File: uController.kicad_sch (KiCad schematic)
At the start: 1 part

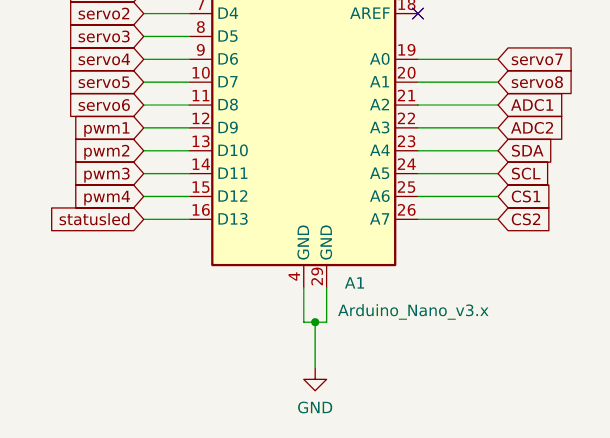
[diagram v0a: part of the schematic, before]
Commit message: redone the switch connectors to accomodate a current sense print. Rearranged parts and updated silk texts to be 50% of their original size
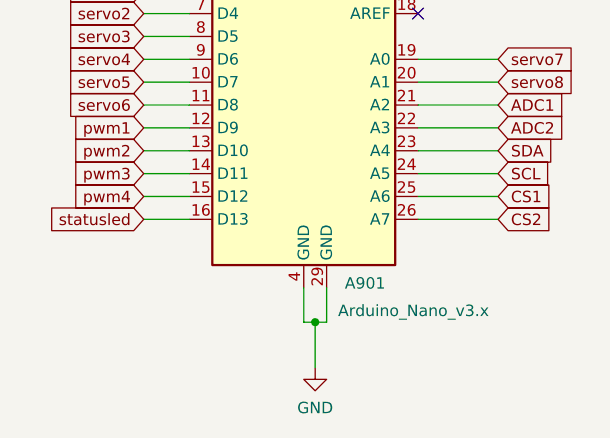
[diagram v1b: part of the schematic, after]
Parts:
- renumbered A1 to A901
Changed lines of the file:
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@@
   (symbol (lib_id "power:GND") (at 149.86 128.27 0) (unit 1)
     (in_bom yes) (on_board yes) (fields_autoplaced)
-    (property "Reference" "#PWR0132" (id 0) (at 149.86 134.62 0)
+    (property "Reference" "#PWR0901" (id 0) (at 149.86 134.62 0)
       (effects (font (size 1.27 1.27)) hide)
     )
@@
   (symbol (lib_id "MCU_Module:Arduino_Nano_v3.x") (at 148.59 93.98 0) (unit 1)
     (in_bom yes) (on_board yes)
-    (property "Reference" "A1" (id 0) (at 153.1494 118.8704 0)
+    (property "Reference" "A901" (id 0) (at 153.1494 118.8704 0)
       (effects (font (size 1.27 1.27)) (justify left))
     )
@@
   (symbol (lib_id "power:+5V") (at 153.67 64.77 0) (unit 1)
     (in_bom yes) (on_board yes) (fields_autoplaced)
-    (property "Reference" "#PWR0141" (id 0) (at 153.67 68.58 0)
+    (property "Reference" "#PWR0902" (id 0) (at 153.67 68.58 0)
       (effects (font (size 1.27 1.27)) hide)
     )

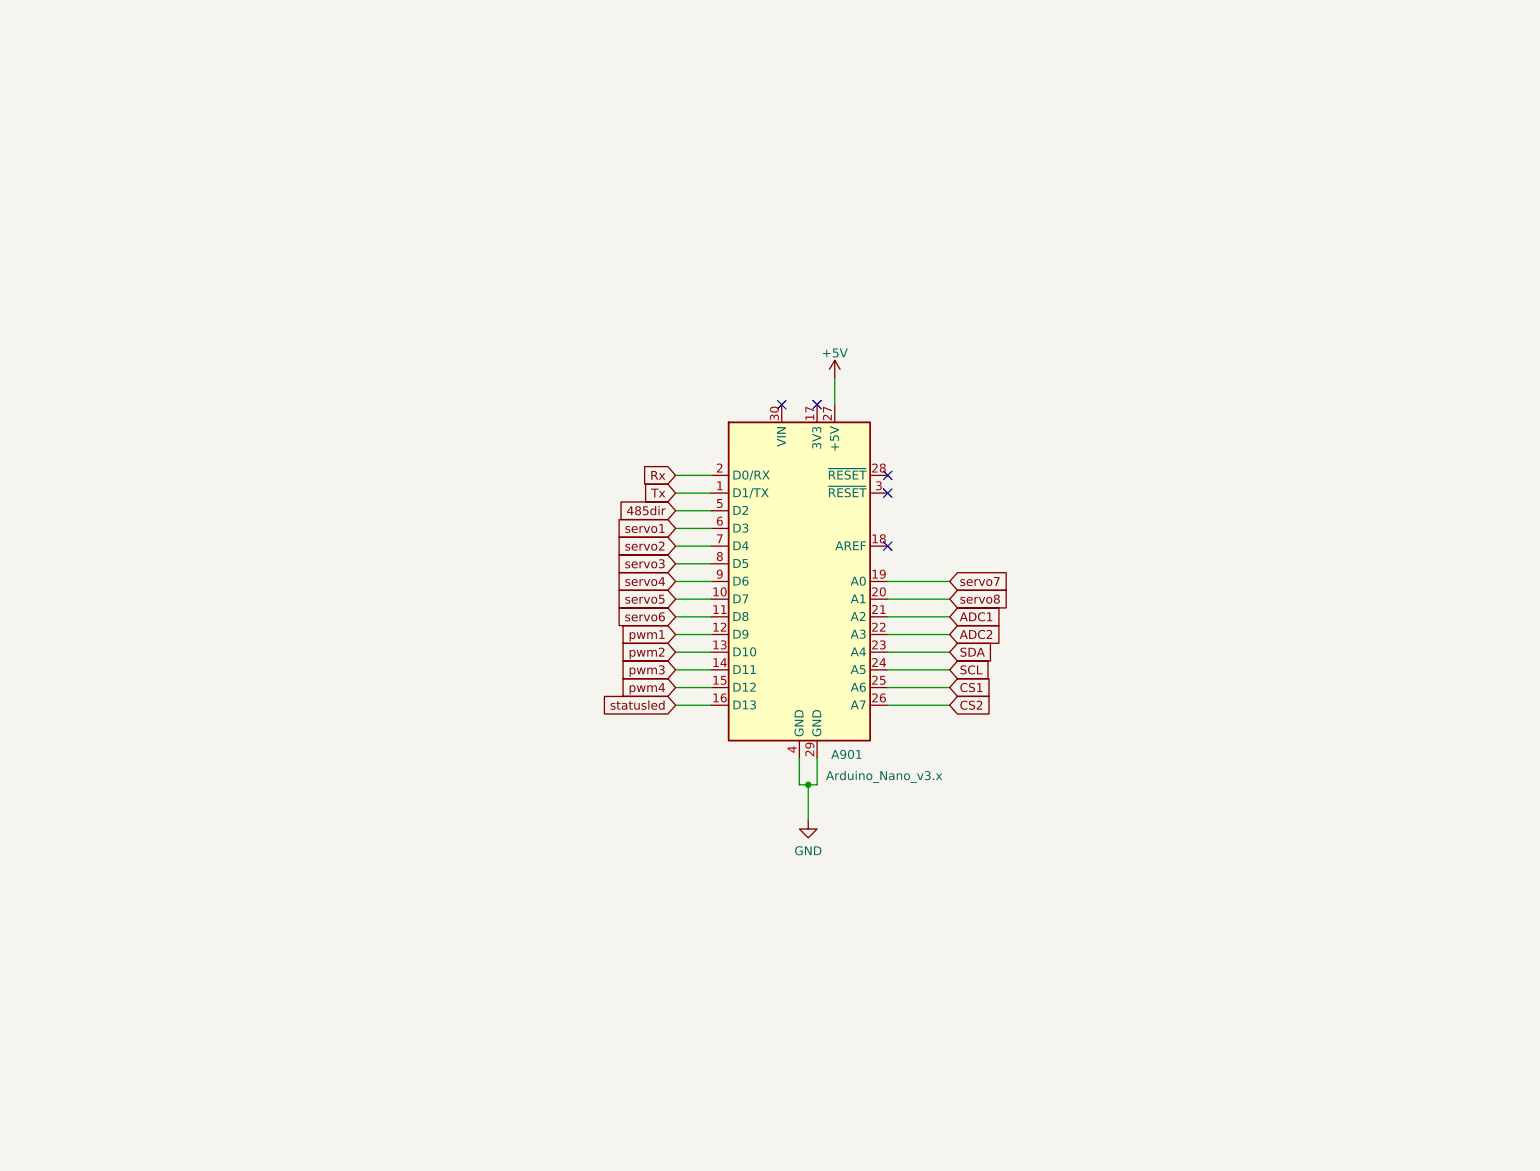
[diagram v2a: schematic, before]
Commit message: altered the code drastically and made a new PCB. PCB is still much work.
I finally fixed that issue where loco functions and speed were not serviced to the multimaus clients.
The Nx code also has been succesfully tested using the monitor.
MCP bug also has been solded. The bug was in assembleIO.py
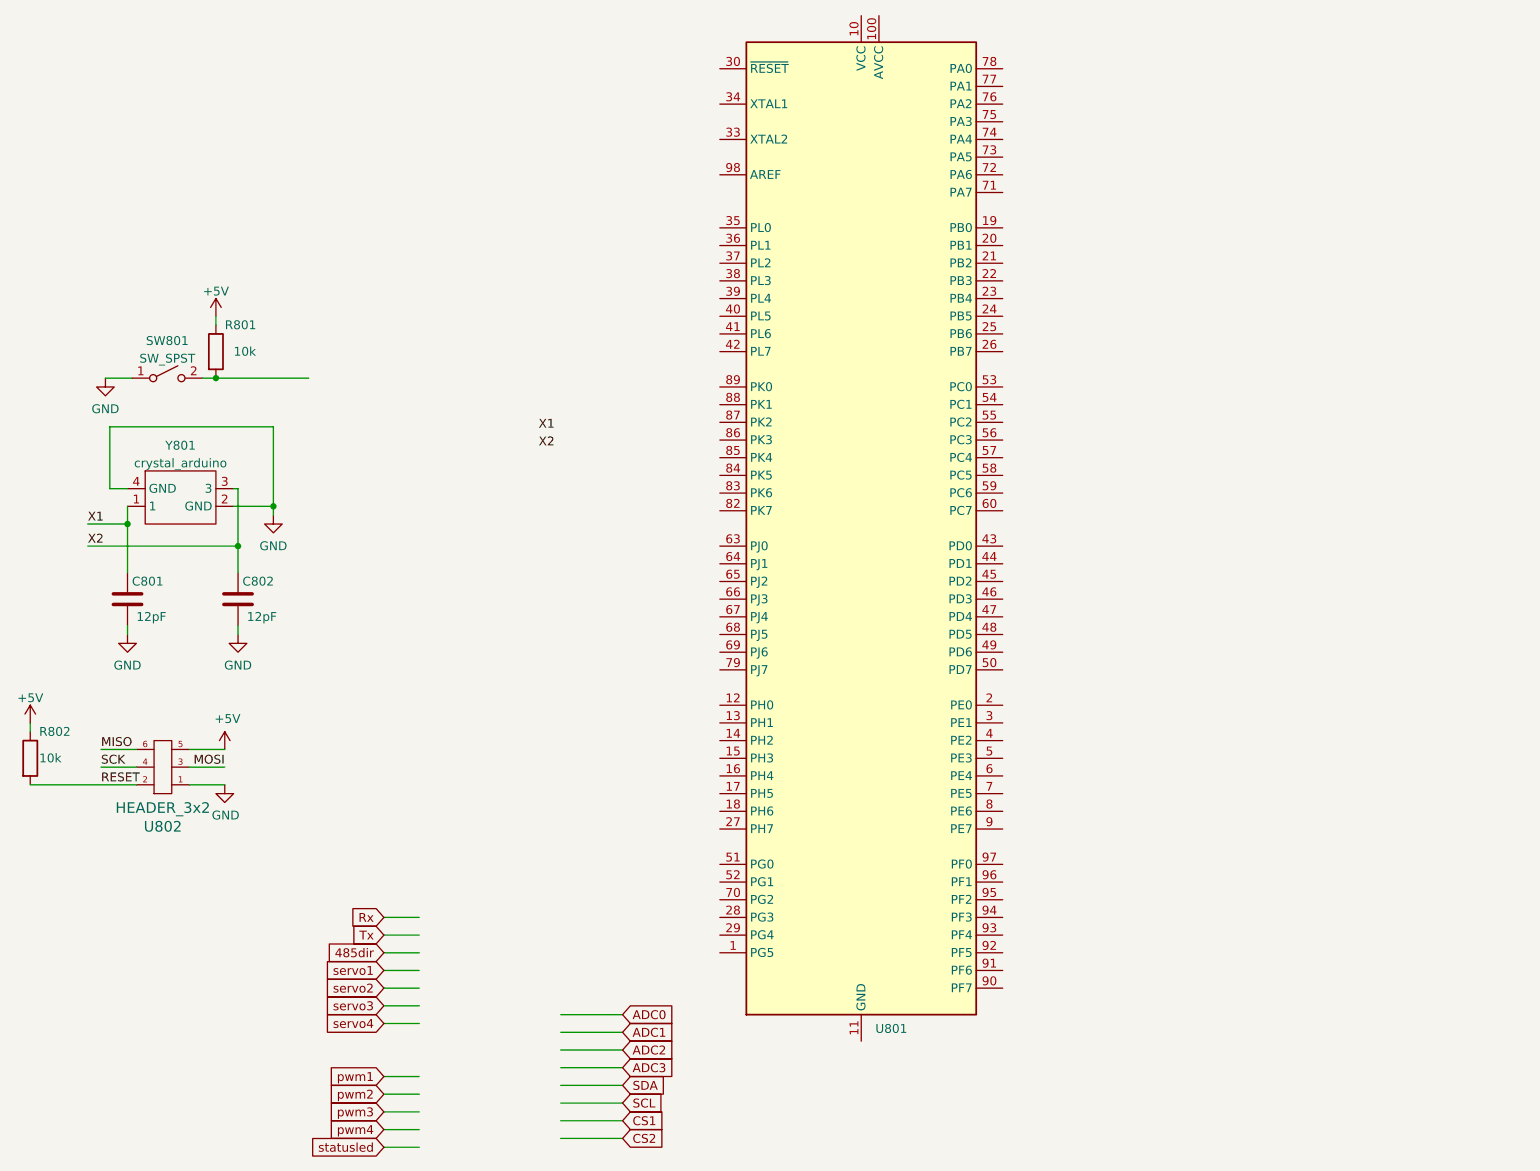
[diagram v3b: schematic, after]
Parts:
- removed A901: Arduino_Nano_v3.x, Module:Arduino_Nano, symbol MCU_Module:Arduino_Nano_v3.x
- added C801, C802: 12pF, Capacitor_SMD:C_0805_2012Metric_Pad1.18x1.45mm_HandSolder, symbol Device:C
- added R801, R802: 10k, Resistor_SMD:R_0805_2012Metric_Pad1.20x1.40mm_HandSolder, symbol Device:R
- added SW801: SW_SPST, Button_Switch_SMD:SW_SPST_SKQG_WithStem, symbol Switch:SW_SPST
- added U801: (no value), symbol MCU_Microchip_ATmega:ATmega2560-16A
- added U802: HEADER_3x2, Connector_PinSocket_1.27mm:PinSocket_2x03_P1.27mm_Vertical, symbol servoDriverSMD-rescue:HEADER_3x2-w_connectors
- added Y801: crystal_arduino, custom_kicad_lib_sk:crystal_arduino, symbol custom_bas:crystal_arduino
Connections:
- net +5V: now also R801.1, R802.1, U802.5
- net GND: now also C801.1, C802.1, SW801.1 (A), U802.1, Y801.2 (GND), Y801.4 (GND)
- new net: R801.2, SW801.2 (B)
- new net: U801.10 (VCC), U801.31 (VCC), U801.61 (VCC), U801.80 (VCC)
- new net: U801.11 (GND), U801.32 (GND), U801.62 (GND), U801.81 (GND), U801.99 (GND)
- new net MISO: U802.6
- new net MOSI: U802.3
- new net RESET: R802.2, U802.2
- new net SCK: U802.4
- new net X1: C801.2, Y801.1
- new net X2: C802.2, Y801.3
- no-connect marks 5 -> 0

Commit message: added missing schematics
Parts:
- U801: value (none) -> ATmega2560-16A; footprint (none) -> Package_QFP:TQFP-100_14x14mm_P0.5mm
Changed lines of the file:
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@@
       (effects (font (size 1.27 1.27)) (justify left))
     )
-    (property "Value" "" (id 1) (at 159.4994 160.7773 0)
+    (property "Value" "ATmega2560-16A" (id 1) (at 159.4994 160.7773 0)
       (effects (font (size 1.27 1.27)) (justify left))
     )
-    (property "Footprint" "" (id 2) (at 157.48 86.36 0)
+    (property "Footprint" "Package_QFP:TQFP-100_14x14mm_P0.5mm" (id 2) (at 157.48 86.36 0)
       (effects (font (size 1.27 1.27) italic) hide)
     )

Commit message: replaced the atmega2560 by an stm32
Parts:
- removed R801: 10k, Resistor_SMD:R_0805_2012Metric_Pad1.20x1.40mm_HandSolder, symbol Device:R
- added U803: (no value), symbol MCU_ST_STM32F1:STM32F103C6Tx
